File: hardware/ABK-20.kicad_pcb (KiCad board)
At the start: 2 copper layers, 90 x 90 mm, 72 parts, among them J1 CONN_01X04, J2 CONN_01X04, J3 CONN_02X03, J4 Con_3-5V, J5 USB_C_6P, J6 Sync_Jumper, SW1 SW_SPST, SW2 SW_Push, SW3 SW_SPDT_MSM, SW4 SW_Push, U1 ATTINY85-20SU, U2 PAM8002, U3 7805

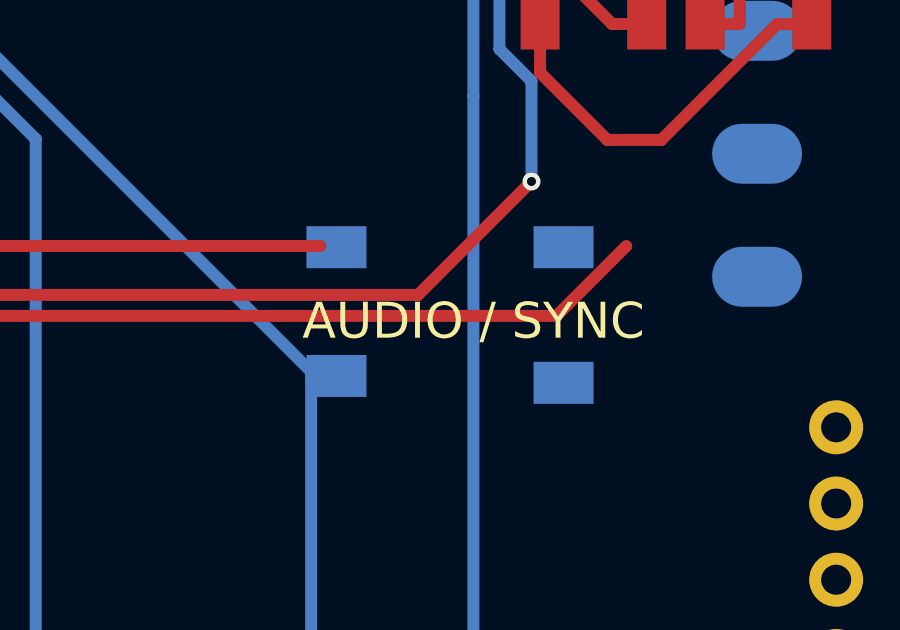
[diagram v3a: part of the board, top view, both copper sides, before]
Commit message: fix(pcb): flip components to F.Cu and correct horizontal audio jack 3D orientation
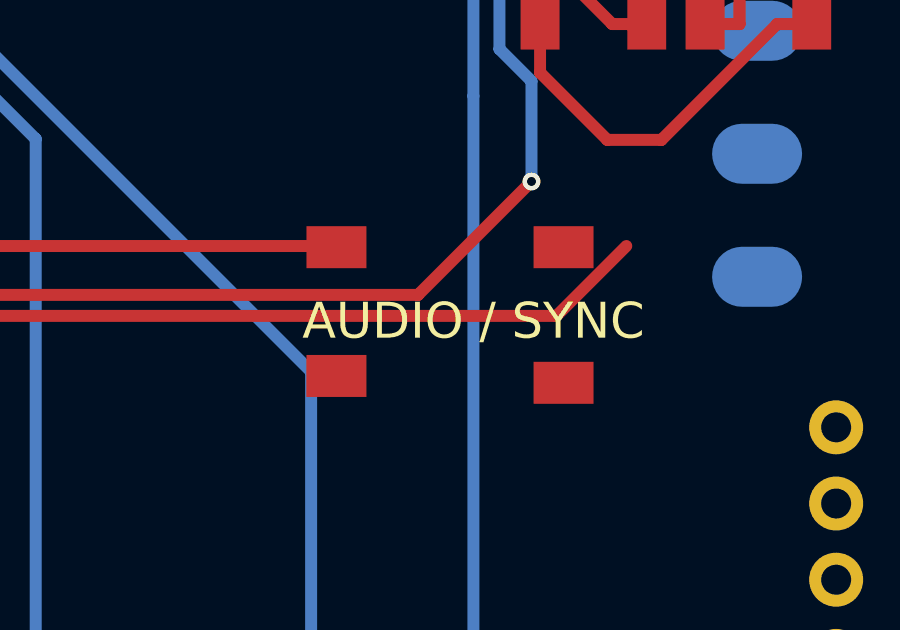
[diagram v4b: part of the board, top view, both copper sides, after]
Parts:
- C1, C2, C3, C4, C5, C6, C7, C8, D1, D2, D3, R1, R10, R11, R12, R13, R14, R15, R16, R17, R18, R2, R3, R4, R5, R6, R7, R8, R9, R99, SW2, U1, U2: moved to F.Cu
- U3: moved to B.Cu
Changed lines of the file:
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@@
 		)
 		(embedded_fonts no)
-		(model "${KIPRJMOD}/3d_models/PJ3410.step"
-			(offset (xyz 0 0 0))
-			(scale (xyz 1 1 1))
-			(rotate (xyz 0 0 0))
+		(model "${KICAD9_3DMODEL_DIR}/Connector_Audio.3dshapes/Jack_3.5mm_CUI_SJ1-3525N_Horizontal.step"
+			(offset
+				(xyz 0 0 0)
+			)
+			(scale
+				(xyz 1 1 1)
+			)
+			(rotate
+				(xyz 0 0 90)
+			)
 		)
 	)
@@
 		)
 		(embedded_fonts no)
-		(model "${KIPRJMOD}/3d_models/PJ3410.step"
-			(offset (xyz 0 0 0))
-			(scale (xyz 1 1 1))
-			(rotate (xyz 0 0 0))
+		(model "${KICAD9_3DMODEL_DIR}/Connector_Audio.3dshapes/Jack_3.5mm_CUI_SJ1-3525N_Horizontal.step"
+			(offset
+				(xyz 0 0 0)
+			)
+			(scale
+				(xyz 1 1 1)
+			)
+			(rotate
+				(xyz 0 0 90)
+			)
 		)
 	)
 	(footprint "Package_TO_SOT_SMD:TO-252-3_TabPin2"
-		(layer "F.Cu")
+		(layer "B.Cu")
 		(at 79.79 34.037)
 		(descr "TO-252/DPAK SMD package, http://www.infineon.com/cms/en/product/packages/PG-TO252/PG-TO252-3-1/")
@@
 	)
 	(footprint "8Bitmixtape_reworked:R_1206_HandSoldering"
-		(layer "B.Cu")
+		(layer "F.Cu")
 		(at 92.11185 90.46405)
 		(descr "Resistor SMD 1206, hand soldering")
@@
 	)
 	(footprint "8Bitmixtape_reworked:C_1206_HandSoldering"
-		(layer "B.Cu")
+		(layer "F.Cu")
 		(at 81.71185 86.66405)
 		(descr "Capacitor SMD 1206, hand soldering")
@@
 	)
 	(footprint "8Bitmixtape_reworked:Attiny_DIP-8_W7.62mm_mod"
-		(layer "B.Cu")
+		(layer "F.Cu")
 		(at 82.169 56.388)
 		(descr "8-lead though-hole mounted DIP package, row spacing 7.62 mm (300 mils)")
@@
 	)
 	(footprint "8Bitmixtape_reworked:C_1206_HandSoldering"
-		(layer "B.Cu")
+		(layer "F.Cu")
 		(at 141.71185 86.66405)
 		(descr "Capacitor SMD 1206, hand soldering")
@@
 	)
 	(footprint "8Bitmixtape_reworked:R_1206_HandSoldering"
-		(layer "B.Cu")
+		(layer "F.Cu")
 		(at 147.21185 94.26405)
 		(descr "Resistor SMD 1206, hand soldering")
@@
 	)
 	(footprint "8Bitmixtape_reworked:R_1206_HandSoldering"
-		(layer "B.Cu")
+		(layer "F.Cu")
 		(at 107.71185 90.46405)
 		(descr "Resistor SMD 1206, hand soldering")
@@
 	)
 	(footprint "8Bitmixtape_reworked:R_1206_HandSoldering"
-		(layer "B.Cu")
+		(layer "F.Cu")
 		(at 102.51185 86.66405)
 		(descr "Resistor SMD 1206, hand soldering")
@@
 	)
 	(footprint "Diode_SMD:D_SMA"
-		(layer "B.Cu")
+		(layer "F.Cu")
 		(at 94.21185 41.66405)
 		(descr "Diode SMA (DO-214AC)")
@@
 	)
 	(footprint "8Bitmixtape_reworked:C_1206_HandSoldering"
-		(layer "B.Cu")
+		(layer "F.Cu")
 		(at 86.91185 86.66405)
 		(descr "Capacitor SMD 1206, hand soldering")
@@
 	)
 	(footprint "8Bitmixtape_reworked:R_1206_HandSoldering"
-		(layer "B.Cu")
+		(layer "F.Cu")
 		(at 81.71185 90.46405)
 		(descr "Resistor SMD 1206, hand soldering")
@@
 	)
 	(footprint "8Bitmixtape_reworked:R_1206_HandSoldering"
-		(layer "B.Cu")
+		(layer "F.Cu")
 		(at 92.11185 94.26405)
 		(descr "Resistor SMD 1206, hand soldering")
@@
 	)
 	(footprint "8Bitmixtape_reworked:C_1206_HandSoldering"
-		(layer "B.Cu")
+		(layer "F.Cu")
 		(at 141.71185 90.46405)
 		(descr "Capacitor SMD 1206, hand soldering")
@@
 	)
 	(footprint "8Bitmixtape_reworked:R_1206_HandSoldering"
-		(layer "B.Cu")
+		(layer "F.Cu")
 		(at 141.71185 94.26405)
 		(descr "Resistor SMD 1206, hand soldering")
@@
 	)
 	(footprint "Diode_SMD:D_SMA"
-		(layer "B.Cu")
+		(layer "F.Cu")
 		(at 88.71185 41.66405)
 		(descr "Diode SMA (DO-214AC)")
@@
 	)
 	(footprint "8Bitmixtape_reworked:SO-8_fixed"
-		(layer "B.Cu")
+		(layer "F.Cu")
 		(at 145.71185 80.66405)
 		(descr "8-Lead Plastic Small Outline, 5.3x6.2mm Body (http://www.ti.com.cn/cn/lit/ds/symlink/tl7705a.pdf)")
@@
 	)
 	(footprint "8Bitmixtape_reworked:R_1206_HandSoldering"
-		(layer "B.Cu")
+		(layer "F.Cu")
 		(at 97.31185 94.26405)
 		(descr "Resistor SMD 1206, hand soldering")
@@
 	)
 	(footprint "8Bitmixtape_reworked:C_1206_HandSoldering"
-		(layer "B.Cu")
+		(layer "F.Cu")
 		(at 147.21185 86.66405)
 		(descr "Capacitor SMD 1206, hand soldering")
@@
 	)
 	(footprint "Diode_SMD:D_SMA"
-		(layer "B.Cu")
+		(layer "F.Cu")
 		(at 77.71185 45.66405)
 		(descr "Diode SMA (DO-214AC)")
@@
 	)
 	(footprint "8Bitmixtape_reworked:R_1206_HandSoldering"
-		(layer "B.Cu")
+		(layer "F.Cu")
 		(at 97.31185 90.46405)
 		(descr "Resistor SMD 1206, hand soldering")
@@
 	)
 	(footprint "8Bitmixtape_reworked:R_1206_HandSoldering"
-		(layer "B.Cu")
+		(layer "F.Cu")
 		(at 102.51185 90.46405)
 		(descr "Resistor SMD 1206, hand soldering")
@@
 	)
 	(footprint "8Bitmixtape_reworked:R_1206_HandSoldering"
-		(layer "B.Cu")
+		(layer "F.Cu")
 		(at 97.31185 86.66405)
 		(descr "Resistor SMD 1206, hand soldering")
@@
 	)
 	(footprint "8Bitmixtape_reworked:R_1206_HandSoldering"
-		(layer "B.Cu")
+		(layer "F.Cu")
 		(at 83.21185 45.66405)
 		(descr "Resistor SMD 1206, hand soldering")
@@
 	)
 	(footprint "8Bitmixtape_reworked:C_1206_HandSoldering"
-		(layer "B.Cu")
+		(layer "F.Cu")
 		(at 147.21185 90.46405)
 		(descr "Capacitor SMD 1206, hand soldering")
@@
 	)
 	(footprint "8Bitmixtape_reworked:R_1206_HandSoldering"
-		(layer "B.Cu")
+		(layer "F.Cu")
 		(at 86.91185 90.46405)
 		(descr "Resistor SMD 1206, hand soldering")
@@
 	)
 	(footprint "8Bitmixtape_reworked:C_1206_HandSoldering"
-		(layer "B.Cu")
+		(layer "F.Cu")
 		(at 77.71185 41.66405)
 		(descr "Capacitor SMD 1206, hand soldering")
@@
 	)
 	(footprint "8Bitmixtape_reworked:R_1206_HandSoldering"
-		(layer "B.Cu")
+		(layer "F.Cu")
 		(at 102.51185 94.26405)
 		(descr "Resistor SMD 1206, hand soldering")
@@
 	)
 	(footprint "8Bitmixtape_reworked:C_1206_HandSoldering"
-		(layer "B.Cu")
+		(layer "F.Cu")
 		(at 83.21185 41.66405)
 		(descr "Capacitor SMD 1206, hand soldering")
@@
 	)
 	(footprint "8Bitmixtape_reworked:R_1206_HandSoldering"
-		(layer "B.Cu")
+		(layer "F.Cu")
 		(at 107.71185 86.66405)
 		(descr "Resistor SMD 1206, hand soldering")
@@
 	)
 	(footprint "8Bitmixtape_reworked:R_1206_HandSoldering"
-		(layer "B.Cu")
+		(layer "F.Cu")
 		(at 88.71185 45.66405)
 		(descr "Resistor SMD 1206, hand soldering")
@@
 	)
 	(footprint "8Bitmixtape_reworked:R_1206_HandSoldering"
-		(layer "B.Cu")
+		(layer "F.Cu")
 		(at 92.11185 86.66405)
 		(descr "Resistor SMD 1206, hand soldering")
@@
 	)
 	(footprint "8Bitmixtape_reworked:TACTILE-PTH_6mm_SMD"
-		(layer "B.Cu")
+		(layer "F.Cu")
 		(at 136.9568 103.9622 180)
 		(descr "OMRON SWITCH")
@@
 			(at -3.7592 2.2606 180)
 			(size 2 1.4)
-			(layers "B.Cu" "B.Mask" "B.Paste")
+			(layers "F.Cu" "F.Mask" "F.Paste")
 			(net 65 "Net-(R16-Pad2)")
 			(pinfunction "1")
@@
 			(at 3.81 2.2606 180)
 			(size 2 1.4)
-			(layers "B.Cu" "B.Mask" "B.Paste")
+			(layers "F.Cu" "F.Mask" "F.Paste")
 			(net 65 "Net-(R16-Pad2)")
 			(pinfunction "1")
@@
 			(at -3.7592 -2.2606 180)
 			(size 2 1.4)
-			(layers "B.Cu" "B.Mask" "B.Paste")
+			(layers "F.Cu" "F.Mask" "F.Paste")
 			(net 3 "GND")
 			(pinfunction "2")
@@
 			(at 3.81 -2.032 180)
 			(size 2 1.4)
-			(layers "B.Cu" "B.Mask" "B.Paste")
+			(layers "F.Cu" "F.Mask" "F.Paste")
 			(net 3 "GND")
 			(pinfunction "2")
@@
 	)
 	(footprint "8Bitmixtape_reworked:R_1206_HandSoldering"
-		(layer "B.Cu")
+		(layer "F.Cu")
 		(at 81.71185 94.26405)
 		(descr "Resistor SMD 1206, hand soldering")
@@
 	)
 	(footprint "8Bitmixtape_reworked:R_1206_HandSoldering"
-		(layer "B.Cu")
+		(layer "F.Cu")
 		(at 86.91185 94.26405)
 		(descr "Resistor SMD 1206, hand soldering")

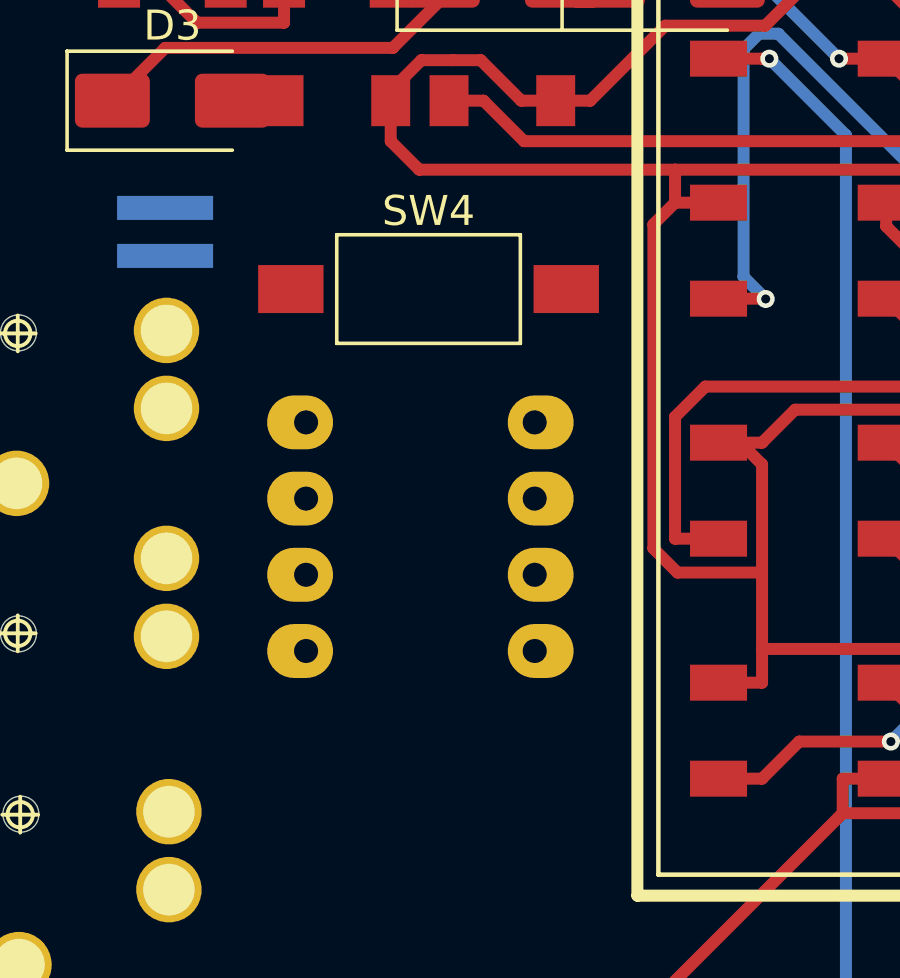
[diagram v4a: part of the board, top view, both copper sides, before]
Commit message: feat(3d-models): create accurate 12x8mm flashlight power switch model (KAN-28)
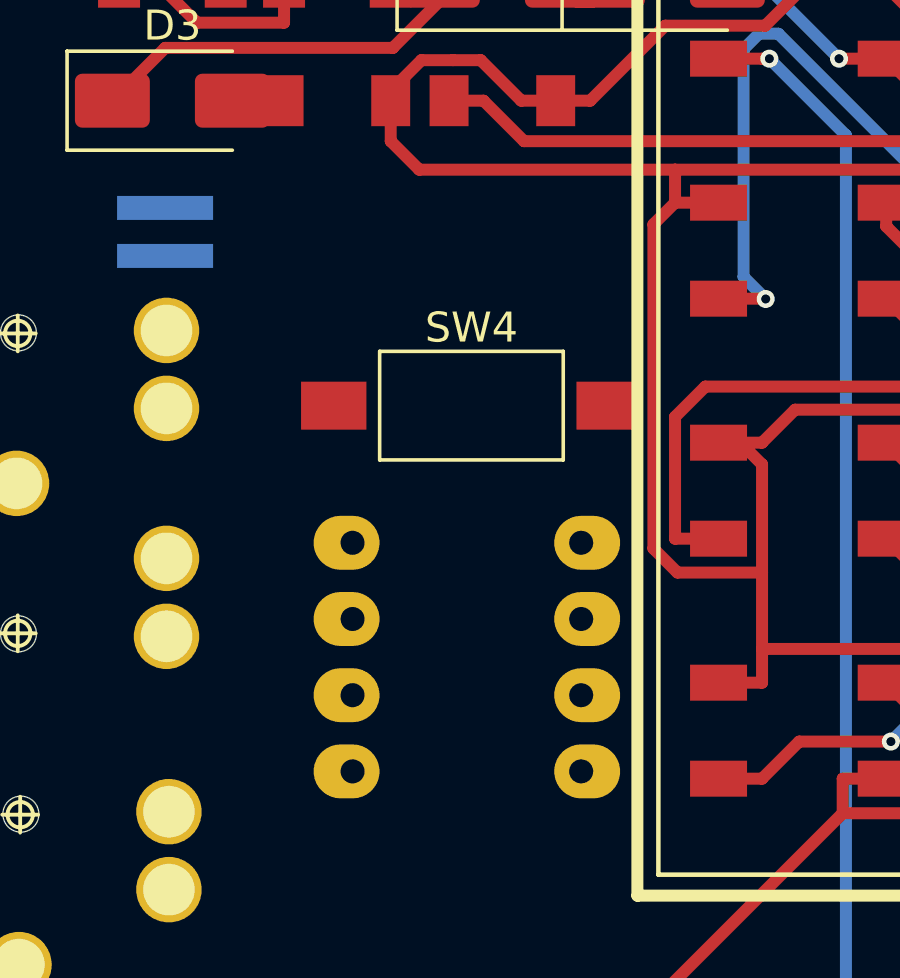
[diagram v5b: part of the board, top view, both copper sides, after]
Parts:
- moved U1 4.30 mm to (83.7, 60.4)
- moved SW4 4.14 mm to (87.7, 55.8)
